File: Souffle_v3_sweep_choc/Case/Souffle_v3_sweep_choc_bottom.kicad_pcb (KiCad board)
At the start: 2 copper layers, 132.1 x 108 mm, 6 parts

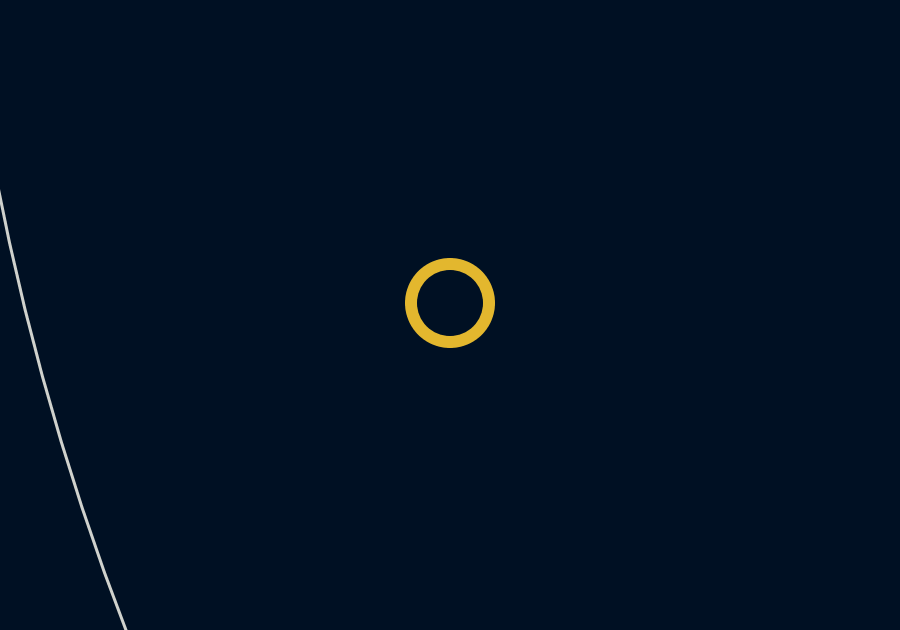
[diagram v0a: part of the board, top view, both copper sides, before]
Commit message: Fixed horizontal spacing of the FN key.
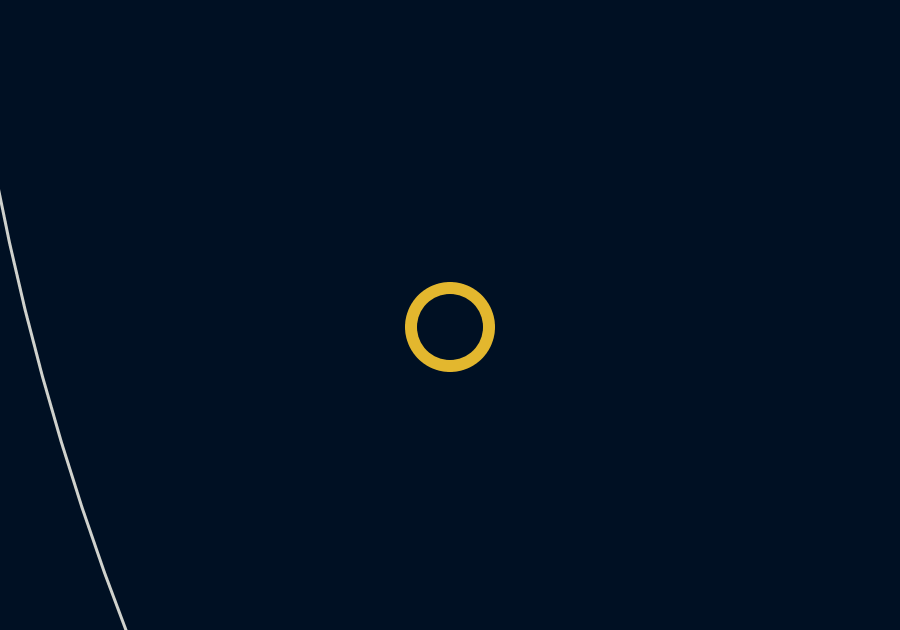
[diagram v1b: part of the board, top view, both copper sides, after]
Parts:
- moved TH2 0.80 mm to (90.6, 111.1)

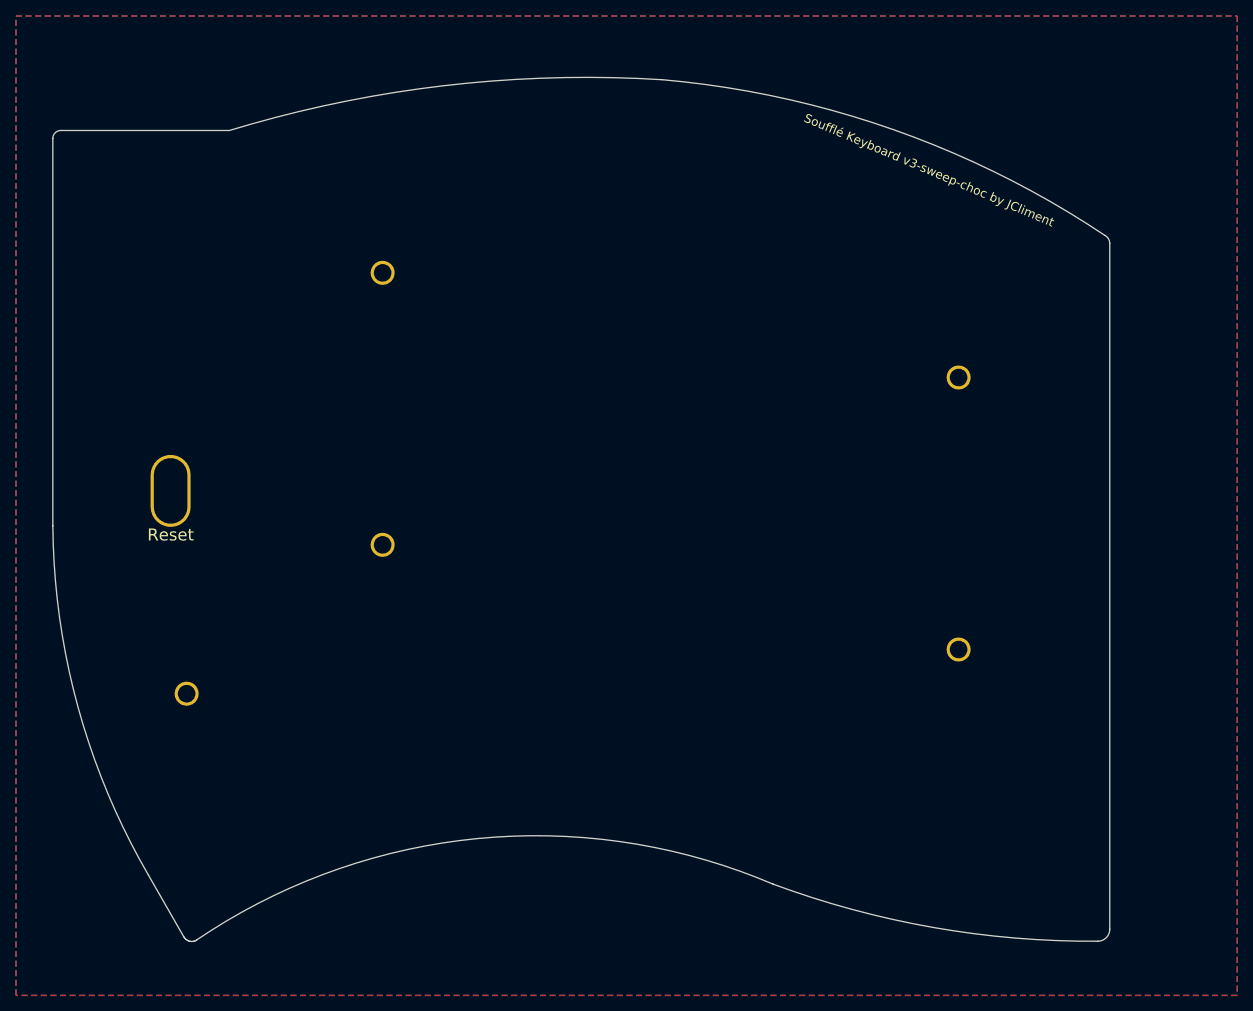
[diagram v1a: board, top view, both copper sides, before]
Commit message: Small changes to make sure the components do not touch each other or the board.
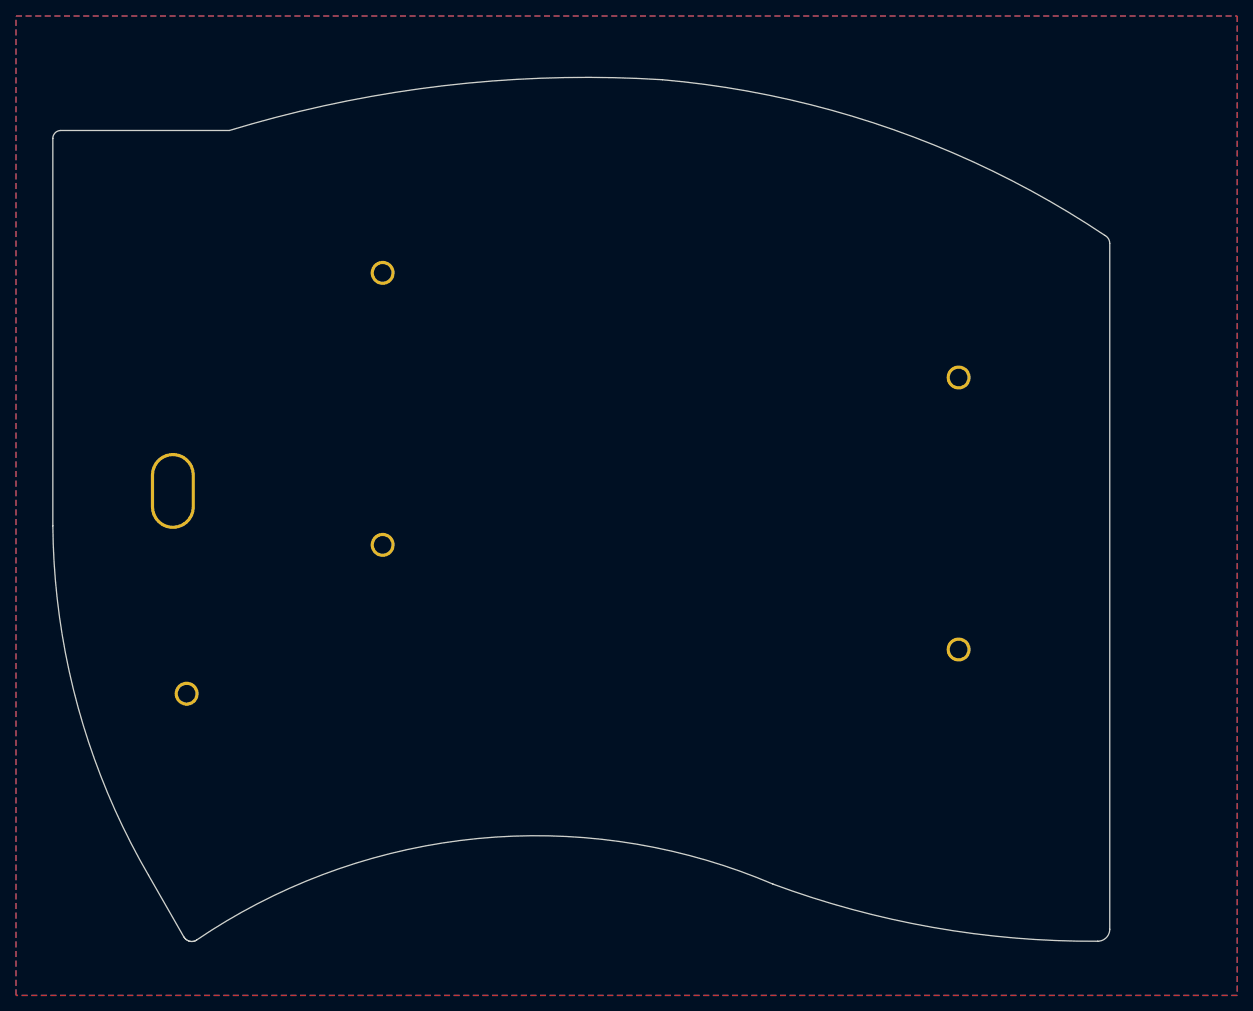
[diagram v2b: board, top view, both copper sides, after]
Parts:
- moved TH2 0.28 mm to (88.9, 85.7)
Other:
- board text removed: "Reset"
- board text removed: "Soufflé Keyboard v3-sweep-choc by JCliment"
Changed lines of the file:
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@@
     )
     (pad_to_mask_clearance 0)
-    (grid_origin 90.634 111.073139)
+    (grid_origin 88.914548 85.727296)
     (pcbplotparams
       (layerselection 0x00010fc_ffffffff)
@@
   )
   (footprint "SofleKeyboard-footprint:M2_HOLE_PCB" locked (layer "F.Cu")
-    (at 88.634 85.723139)
+    (at 88.914548 85.727296)
     (property "Sheetfile" "Souffle_v2.kicad_sch")
     (property "Sheetname" "")
@@
       (effects (font (size 1 1) (thickness 0.15)))
     )
-    (pad "" thru_hole oval locked (at 0 0) (size 5 9) (drill oval 4.2 8.2) (layers *.Cu *.Mask "Dwgs.User"))
+    (pad "" thru_hole oval locked (at 0 0) (size 5.5 9.5) (drill oval 4.7 8.7) (layers *.Cu *.Mask "Dwgs.User"))
   )
   (footprint "SofleKeyboard-footprint:M2_HOLE_PCB" locked (layer "F.Cu")
@@
     (pad "" thru_hole circle locked (at 0 0) (size 3 3) (drill 2.2) (layers F&B.Cu *.Mask "Dwgs.User"))
   )
-  (gr_line locked (start 210.617591 139.690824) (end 210.437331 139.801743) (layer "Cmts.User") (width 0.1))
   (gr_line locked (start 90.720149 141.899419) (end 90.552207 141.785459) (layer "Cmts.User") (width 0.1))
+  (gr_line (start 206.023354 54.787504) (end 206.023354 140.512504) (layer "Cmts.User") (width 0.1))
   (gr_line locked (start 90.283386 141.469069) (end 85.872 133.769139) (layer "Cmts.User") (width 0.1))
-  (gr_arc locked (start 91.881794 141.860999) (mid 123.551225 129.412239) (end 157.5 131.737139) (layer "Cmts.User") (width 0.1))
   (gr_line locked (start 90.904246 141.981719) (end 90.720149 141.899419) (layer "Cmts.User") (width 0.1))
-  (gr_line locked (start 211.005907 49.404665) (end 211.060007 49.600564) (layer "Cmts.User") (width 0.1))
-  (gr_line locked (start 210.997481 139.194474) (end 210.901481 139.383074) (layer "Cmts.User") (width 0.1))
   (gr_line locked (start 91.709202 141.962619) (end 91.881794 141.860999) (layer "Cmts.User") (width 0.1))
-  (gr_arc locked (start 73.907857 37.700709) (mid 74.20075 36.993602) (end 74.907857 36.700709) (layer "Cmts.User") (width 0.1))
+  (gr_arc (start 91.881794 141.860999) (mid 127.016544 129.176284) (end 163.934 134.873139) (layer "Cmts.User") (width 0.1))
+  (gr_arc locked (start 73.907857 41.669459) (mid 74.200744 40.962331) (end 74.907857 40.669459) (layer "Cmts.User") (width 0.1))
   (gr_line locked (start 91.506976 142.022919) (end 91.302308 142.045119) (layer "Cmts.User") (width 0.1))
-  (gr_line locked (start 210.919507 49.2238) (end 211.005907 49.404665) (layer "Cmts.User") (width 0.1))
-  (gr_line locked (start 210.497497 48.807459) (end 210.662247 48.921593) (layer "Cmts.User") (width 0.1))
-  (gr_line locked (start 210.662247 48.921593) (end 210.803947 49.061575) (layer "Cmts.User") (width 0.1))
-  (gr_line locked (start 211.0717 138.779939) (end 211.057881 138.988205) (layer "Cmts.User") (width 0.1))
-  (gr_line locked (start 210.437331 139.801743) (end 210.236601 139.878543) (layer "Cmts.User") (width 0.1))
+  (gr_arc (start 206.023354 140.512504) (mid 205.583973 141.573123) (end 204.523354 142.012504) (layer "Cmts.User") (width 0.1))
+  (gr_line (start 95.983431 40.669459) (end 74.907857 40.669459) (layer "Cmts.User") (width 0.1))
   (gr_line locked (start 90.552207 141.785459) (end 90.40507 141.641469) (layer "Cmts.User") (width 0.1))
+  (gr_line (start 73.909257 90.081139) (end 73.907857 41.669459) (layer "Cmts.User") (width 0.1))
   (gr_arc locked (start 85.872 133.769139) (mid 77.043897 112.704637) (end 73.909257 90.081139) (layer "Cmts.User") (width 0.1))
-  (gr_arc locked (start 144.3715 29.329389) (mid 178.787348 34.438498) (end 210.479413 48.796999) (layer "Cmts.User") (width 0.1))
-  (gr_line locked (start 211.057881 138.988205) (end 210.997481 139.194474) (layer "Cmts.User") (width 0.1))
-  (gr_arc locked (start 209.535 139.935639) (mid 186.721075 138.503894) (end 164.358 133.769139) (layer "Cmts.User") (width 0.1))
-  (gr_line locked (start 210.019191 139.917143) (end 209.7636 139.935639) (layer "Cmts.User") (width 0.1))
-  (gr_line locked (start 210.901481 139.383074) (end 210.773571 139.549894) (layer "Cmts.User") (width 0.1))
-  (gr_line locked (start 211.060007 49.600564) (end 211.078807 49.807895) (layer "Cmts.User") (width 0.1))
-  (gr_line locked (start 210.803947 49.061575) (end 210.919507 49.2238) (layer "Cmts.User") (width 0.1))
-  (gr_line locked (start 211.077181 49.793234) (end 211.0717 138.779939) (layer "Cmts.User") (width 0.1))
   (gr_line locked (start 91.099848 142.030819) (end 90.904246 141.981719) (layer "Cmts.User") (width 0.1))
-  (gr_arc locked (start 210.479413 48.796999) (mid 210.913598 49.213932) (end 211.077181 49.793234) (layer "Cmts.User") (width 0.1))
-  (gr_arc locked (start 95.983431 36.700709) (mid 119.878864 31.054919) (end 144.3715 29.329389) (layer "Cmts.User") (width 0.1))
-  (gr_line locked (start 210.773571 139.549894) (end 210.617591 139.690824) (layer "Cmts.User") (width 0.1))
+  (gr_arc (start 205.425586 53.791269) (mid 205.859748 54.208216) (end 206.023354 54.787504) (layer "Cmts.User") (width 0.1))
+  (gr_arc (start 150.107857 34.323659) (mid 178.994956 40.567403) (end 205.425586 53.791269) (layer "Cmts.User") (width 0.1))
   (gr_line locked (start 91.709202 141.962619) (end 91.506976 142.022919) (layer "Cmts.User") (width 0.1))
-  (gr_line locked (start 164.358 133.769139) (end 157.5 131.737139) (layer "Cmts.User") (width 0.1))
   (gr_line locked (start 90.40507 141.641469) (end 90.283386 141.469069) (layer "Cmts.User") (width 0.1))
-  (gr_line locked (start 73.909257 90.081139) (end 73.907857 37.700709) (layer "Cmts.User") (width 0.1))
-  (gr_line locked (start 95.983431 36.700709) (end 74.907857 36.700709) (layer "Cmts.User") (width 0.1))
-  (gr_line locked (start 209.7636 139.935639) (end 209.535 139.935639) (layer "Cmts.User") (width 0.1))
-  (gr_line locked (start 210.236601 139.878543) (end 210.019191 139.917143) (layer "Cmts.User") (width 0.1))
+  (gr_arc (start 204.523354 142.012504) (mid 183.905135 140.282251) (end 163.934 134.873139) (layer "Cmts.User") (width 0.1))
+  (gr_arc (start 95.983431 40.669459) (mid 122.761645 35.07428) (end 150.107857 34.323659) (layer "Cmts.User") (width 0.1))
   (gr_line locked (start 91.302308 142.045119) (end 91.099848 142.030819) (layer "Cmts.User") (width 0.1))
   (gr_line locked (start 90.40507 141.641469) (end 90.283386 141.469069) (layer "Edge.Cuts") (width 0.1))
@@
   (gr_arc locked (start 204.523354 142.012504) (mid 183.905135 140.282251) (end 163.934 134.873139) (layer "Edge.Cuts") (width 0.1))
   (gr_line locked (start 90.552207 141.785459) (end 90.40507 141.641469) (layer "Edge.Cuts") (width 0.1))
-  (gr_text "Soufflé Keyboard v3-sweep-choc by JCliment" (at 183.445357 45.638209 -23) (layer "B.SilkS")
-    (effects (font (size 1.1 1.1) (thickness 0.2)) (justify mirror))
-  )
-  (gr_text "Reset" (at 88.634 91.223139) (layer "B.SilkS")
-    (effects (font (size 1.5 1.5) (thickness 0.3)) (justify mirror))
-  )
-  (gr_text "Soufflé Keyboard v3-sweep-choc by JCliment" (at 183.445357 45.638209 -23) (layer "F.SilkS")
-    (effects (font (size 1.1 1.1) (thickness 0.2)))
-  )
-  (gr_text "Reset" (at 88.634 91.223139) (layer "F.SilkS")
-    (effects (font (size 1.5 1.5) (thickness 0.3)))
-  )
   (zone locked (net 1) (net_name "GND") (layers F&B.Cu) (hatch edge 0.508)
     (connect_pads (clearance 0.508))
